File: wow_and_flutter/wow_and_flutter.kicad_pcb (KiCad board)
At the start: 2 copper layers, 127 x 128.5 mm, 72 parts, among them J1 EURO POWER, J2 OUTPUT, J3 B1_POWER, J4 B2_POWER, J5 B1_SIGNAL, J6 B2_SIGNAL, Q1 2N3904, Q2 J113, Q3 2N3904, SW1 SW_SPDT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

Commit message: Complete PCB laout
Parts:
- C3, C4, C5, C6: value 0.1uF -> 100nF
- J5: footprint Connector_PinHeader_2.54mm:PinHeader_1x07_P2.54mm_Vertical -> Connector_PinHeader_2.54mm:PinHeader_1x06_P2.54mm_Vertical
- J6: footprint Connector_PinSocket_2.54mm:PinSocket_1x07_P2.54mm_Vertical -> Connector_PinSocket_2.54mm:PinSocket_1x06_P2.54mm_Vertical
- moved C10 136.6 mm to (182.9, 114.3)
- moved C9 134.5 mm to (180.3, 108.6), turned to -90 degrees
- moved Q2 119.4 mm to (184.8, 81.9), turned to -90 degrees
- moved R16 118.5 mm to (182.9, 101.0), turned to 90 degrees
- moved C8 117.6 mm to (194.3, 115.2), turned to 90 degrees
- moved D1 109.3 mm to (200.7, 76.2), turned to 90 degrees
- moved C11 106.6 mm to (200.7, 108.6), turned to -90 degrees
- moved C3 104.2 mm to (188.0, 113.7)
- moved R17 102.9 mm to (180.3, 83.2), turned to -90 degrees
- moved R7 100.8 mm to (198.1, 127.6), turned to 90 degrees
- moved R8 97.4 mm to (188.0, 117.5), turned to -90 degrees
- moved C4 95.9 mm to (190.5, 98.5), turned to -90 degrees
- moved R18 95.1 mm to (195.6, 90.8), turned to -90 degrees
- moved R14 94.8 mm to (188.0, 101.0), turned to 90 degrees
- moved R9 91.6 mm to (185.4, 127.6), turned to 90 degrees
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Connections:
- net Net-(C12-Pad1) renamed /TRIG_FILTER
- net Net-(C8-Pad1) renamed /NOISE_SRC
- net Net-(D2-Pad2) renamed /SH_GATE
- net Net-(U1-Pad1) renamed /NOISE_AMP1
- net Net-(U1-Pad2) renamed /NOISE_AMP1_FB
- net Net-(U1-Pad3) renamed /NOISE_IN
- net Net-(U1-Pad5) renamed /NOISE_AMP2
- net Net-(U1-Pad6) renamed /NOISE_AMP2_FB
- net Net-(U2-Pad13) renamed /GAIN_SELECT
- C13 pad 2: Net-(U1-Pad12) -> /SH_IN
- C14 pad 1: Net-(U1-Pad13) -> /SH_FB
- C3 pad 1: +12V -> GND
- C3 pad 2: GND -> +12V
- C5 pad 1: +12V -> GND
- C5 pad 2: GND -> +12V
- D1 pad 1: Net-(U1-Pad10) -> /TRIG_IN
- J5 pad 2: /S&H -> /DEPTH_FB
- J5 pad 3: /DEPTH_FB -> /DEPTH_CTRL
- J5 pad 4: /DEPTH_CTRL -> /S&H
- J5 pad 5: /SLEW_OUT -> /LFO_FB
- J5 pad 6: /LFO_FB -> /LFO_CTRL
- J6 pad 2: /S&H -> /DEPTH_FB
- J6 pad 3: /DEPTH_FB -> /DEPTH_CTRL
- J6 pad 4: /DEPTH_CTRL -> /S&H
- J6 pad 5: /SLEW_OUT -> /LFO_FB
- J6 pad 6: /LFO_FB -> /LFO_CTRL
- Q2 pad 2: Net-(U1-Pad12) -> /SH_IN
- R14 pad 1: Net-(U1-Pad10) -> /TRIG_IN
- R15 pad 2: Net-(U1-Pad9) -> /TRIG_CMP
- R16 pad 1: Net-(U1-Pad9) -> /TRIG_CMP
- R18 pad 2: Net-(U1-Pad13) -> /SH_FB
- R19 pad 1: Net-(U1-Pad13) -> /SH_FB
- R20 pad 1: Net-(R20-Pad1) -> /INV_OUT
- R3 pad 2: Net-(R3-Pad2) -> /LFO_CMP
- R4 pad 1: Net-(R3-Pad2) -> /LFO_CMP
- U1 pad 10: Net-(U1-Pad10) -> /SH_IN
- U1 pad 12: Net-(U1-Pad12) -> /TRIG_IN
- U1 pad 13: Net-(U1-Pad13) -> /TRIG_CMP
- U1 pad 14: /S&H -> /SH_TRIG
- U1 pad 8: /SH_TRIG -> /S&H
- U1 pad 9: Net-(U1-Pad9) -> /SH_FB
- U2 pad 1: /TRI -> /INV_OUT
- U2 pad 10: /DEPTH_CTRL -> /LFO_CMP
- U2 pad 2: /LFO_CTRL -> /INV_OUT
- U2 pad 3: GND -> /DEPTH_CTRL
- U2 pad 5: Net-(R3-Pad2) -> GND
- U2 pad 6: GND -> /LFO_CTRL
- U2 pad 7: /SQR -> /TRI
- U2 pad 8: Net-(R20-Pad1) -> /SQR
- U2 pad 9: Net-(R20-Pad1) -> GND
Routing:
- net -12V: track 22.4 -> 152.5 mm, vias 0 -> 2
- net +12V: track 23.9 -> 132.4 mm, vias 0 -> 1
- net /NOISE: track 0.00 -> 53.7 mm, vias 0 -> 1
- net /NOISE_AMP2_FB: track 0.00 -> 46.1 mm, vias 0 -> 1
- net /TRIG_IN: track 0.00 -> 40.6 mm, vias 0 -> 1
- net /TRI: track 42.6 -> 81.1 mm, vias 0 -> 2
- net /S&H: track 19.7 -> 51.7 mm
- net /SH_IN: track 0.00 -> 26.0 mm
- net /LFO_FB: track 45.2 -> 70.4 mm
- net /NOISE_AMP1_FB: track 0.00 -> 24.3 mm
- net /DEPTH_FB: track 85.4 -> 107.0 mm
- net /SH_FB: track 0.00 -> 19.9 mm, vias 0 -> 1
- net /SLEW_OUT: track 50.9 -> 32.1 mm
- net /NOISE_AMP2: track 0.00 -> 16.3 mm
- net /NOISE_IN: track 0.00 -> 14.8 mm
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
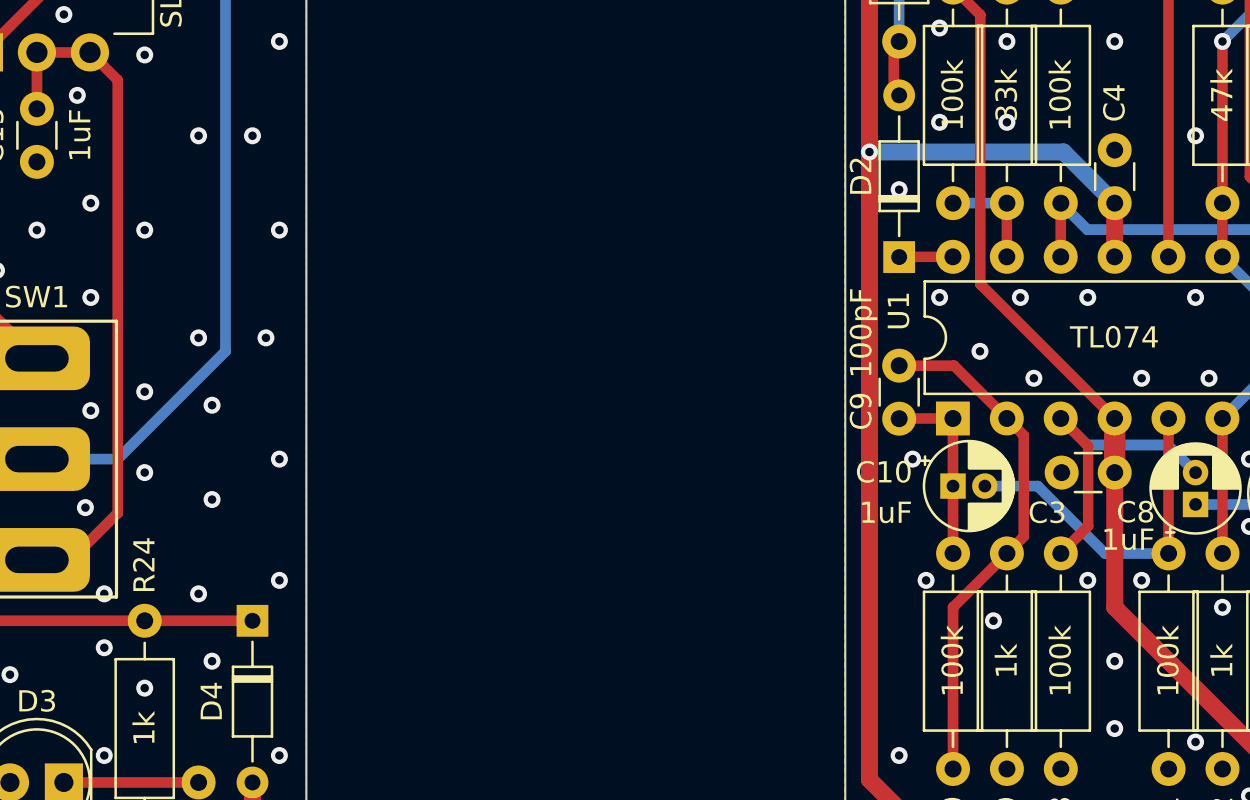
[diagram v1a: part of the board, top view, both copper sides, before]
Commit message: Add version info to PCBs
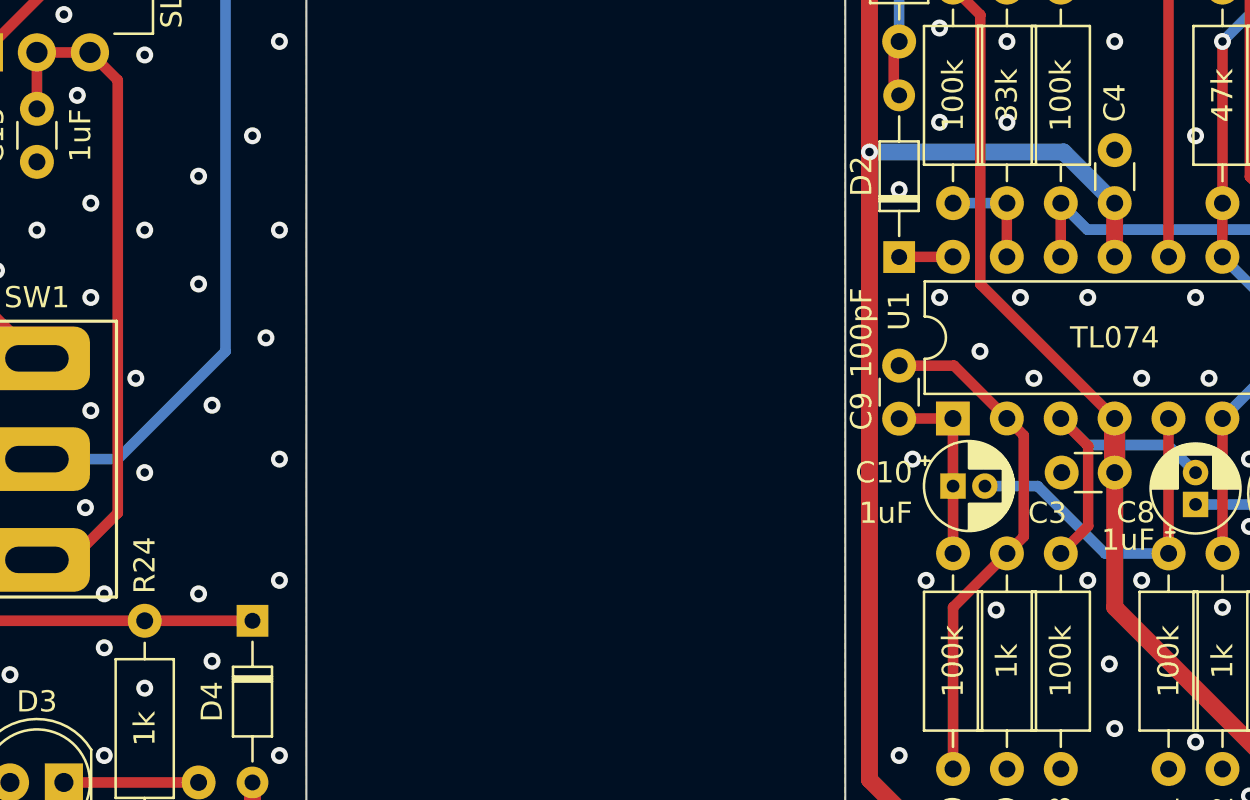
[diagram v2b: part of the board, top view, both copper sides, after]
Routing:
- net GND: vias 247 -> 246
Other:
- board text added: "WOW & FLUTTER Connector Board Max Proskauer v0.1 Feb 2023 github.com/mprosk/wow_and_flutter"
- board text added: "WOW & FLUTTER Front Panel Max Proskauer v0.1 Feb 2023 github.com/mprosk/wow_and_flutter"
- board text added: "WOW & FLUTTER Mainboard Max Proskauer v0.1 Feb 2023 github.com/mprosk/wow_and_flutter"
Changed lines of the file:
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@@
+    (effects (font (size 1 1) (thickness 0.15)) (justify mirror))
+  )
+  (gr_text "WOW & FLUTTER Connector Board\nMax Proskauer  v0.1  Feb 2023\ngithub.com/mprosk/wow_and_flutter" (at 147.32 104.14 270) (layer "B.SilkS")
     (effects (font (size 1 1) (thickness 0.15)) (justify mirror))
   )
   (gr_text "±5V SYNTH LEVEL" (at 186.69 34.925) (layer "B.SilkS")
+    (effects (font (size 1 1) (thickness 0.15)) (justify mirror))
+  )
+  (gr_text "WOW & FLUTTER Mainboard\nMax Proskauer  v0.1  Feb 2023\ngithub.com/mprosk/wow_and_flutter" (at 189.865 122.555) (layer "B.SilkS")
+    (effects (font (size 0.8 0.8) (thickness 0.12)) (justify mirror))
+  )
+  (gr_text "WOW & FLUTTER Front Panel\nMax Proskauer  v0.1  Feb 2023\ngithub.com/mprosk/wow_and_flutter" (at 91.44 99.06) (layer "B.SilkS")
     (effects (font (size 1 1) (thickness 0.15)) (justify mirror))
   )
@@
   (via (at 137.16 131.445) (size 0.8) (drill 0.4) (layers "F.Cu" "B.Cu") (free) (net 2))
   (via (at 149.225 139.065) (size 0.8) (drill 0.4) (layers "F.Cu" "B.Cu") (free) (net 2))
-  (via (at 190.5 122.555) (size 0.8) (drill 0.4) (layers "F.Cu" "B.Cu") (free) (net 2))
+  (via (at 190.246 122.682) (size 0.8) (drill 0.4) (layers "F.Cu" "B.Cu") (free) (net 2))
   (via (at 142.24 78.105) (size 0.8) (drill 0.4) (layers "F.Cu" "B.Cu") (free) (net 2))
   (via (at 201.93 59.69) (size 0.8) (drill 0.4) (layers "F.Cu" "B.Cu") (free) (net 2))
@@
   (via (at 181.61 45.72) (size 0.8) (drill 0.4) (layers "F.Cu" "B.Cu") (free) (net 2))
   (via (at 179.07 139.7) (size 0.8) (drill 0.4) (layers "F.Cu" "B.Cu") (free) (net 2))
-  (via (at 147.32 97.79) (size 0.8) (drill 0.4) (layers "F.Cu" "B.Cu") (free) (net 2))
+  (via (at 147.32 99.695) (size 0.8) (drill 0.4) (layers "F.Cu" "B.Cu") (free) (net 2))
   (via (at 185.42 65.405) (size 0.8) (drill 0.4) (layers "F.Cu" "B.Cu") (free) (net 2))
   (via (at 183.515 134.62) (size 0.8) (drill 0.4) (layers "F.Cu" "B.Cu") (free) (net 2))
@@
   (via (at 199.39 33.02) (size 0.8) (drill 0.4) (layers "F.Cu" "B.Cu") (free) (net 2))
   (via (at 198.12 98.425) (size 0.8) (drill 0.4) (layers "F.Cu" "B.Cu") (free) (net 2))
-  (via (at 144.78 109.855) (size 0.8) (drill 0.4) (layers "F.Cu" "B.Cu") (free) (net 2))
+  (via (at 144.3595 109.22) (size 0.8) (drill 0.4) (layers "F.Cu" "B.Cu") (free) (net 2))
   (via (at 201.93 129.54) (size 0.8) (drill 0.4) (layers "F.Cu" "B.Cu") (free) (net 2))
   (via (at 191.77 59.69) (size 0.8) (drill 0.4) (layers "F.Cu" "B.Cu") (free) (net 2))
@@
   (via (at 128.27 55.88) (size 0.8) (drill 0.4) (layers "F.Cu" "B.Cu") (free) (net 2))
   (via (at 195.58 86.995) (size 0.8) (drill 0.4) (layers "F.Cu" "B.Cu") (free) (net 2))
-  (via (at 147.955 114.935) (size 0.8) (drill 0.4) (layers "F.Cu" "B.Cu") (free) (net 2))
   (via (at 128.27 130.175) (size 0.8) (drill 0.4) (layers "F.Cu" "B.Cu") (free) (net 2))
   (via (at 135.255 97.155) (size 0.8) (drill 0.4) (layers "F.Cu" "B.Cu") (free) (net 2))
@@
   (via (at 195.58 33.02) (size 0.8) (drill 0.4) (layers "F.Cu" "B.Cu") (free) (net 2))
   (via (at 128.27 79.375) (size 0.8) (drill 0.4) (layers "F.Cu" "B.Cu") (free) (net 2))
-  (via (at 184.785 120.65) (size 0.8) (drill 0.4) (layers "F.Cu" "B.Cu") (free) (net 2))
+  (via (at 184.912 120.142) (size 0.8) (drill 0.4) (layers "F.Cu" "B.Cu") (free) (net 2))
   (via (at 142.875 127) (size 0.8) (drill 0.4) (layers "F.Cu" "B.Cu") (free) (net 2))
   (via (at 144.78 113.665) (size 0.8) (drill 0.4) (layers "F.Cu" "B.Cu") (free) (net 2))
   (via (at 190.5 50.8) (size 0.8) (drill 0.4) (layers "F.Cu" "B.Cu") (free) (net 2))
-  (via (at 147.32 107.315) (size 0.8) (drill 0.4) (layers "F.Cu" "B.Cu") (free) (net 2))
+  (via (at 147.32 104.775) (size 0.8) (drill 0.4) (layers "F.Cu" "B.Cu") (free) (net 2))
   (via (at 195.58 120.015) (size 0.8) (drill 0.4) (layers "F.Cu" "B.Cu") (free) (net 2))
   (via (at 131.445 121.92) (size 0.8) (drill 0.4) (layers "F.Cu" "B.Cu") (free) (net 2))
